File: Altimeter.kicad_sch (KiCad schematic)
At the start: 44 parts, among them U1 ESP32-S3, Y1 40MHz±10ppm

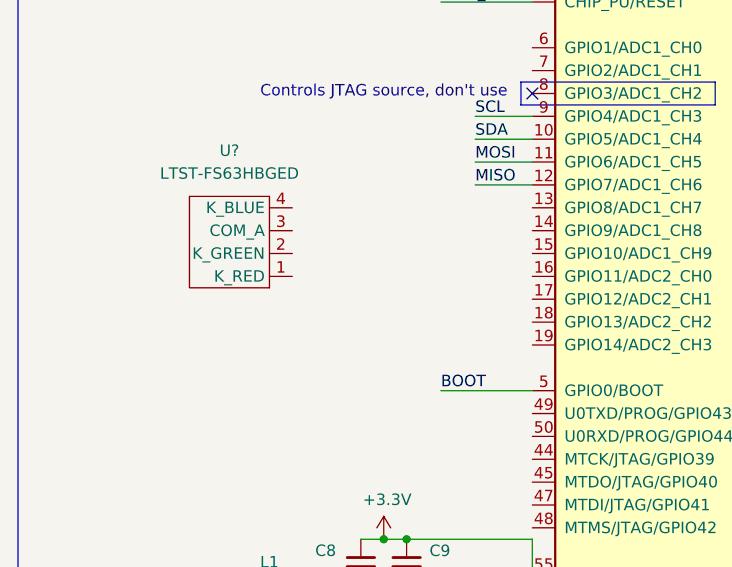
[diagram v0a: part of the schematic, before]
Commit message: added led
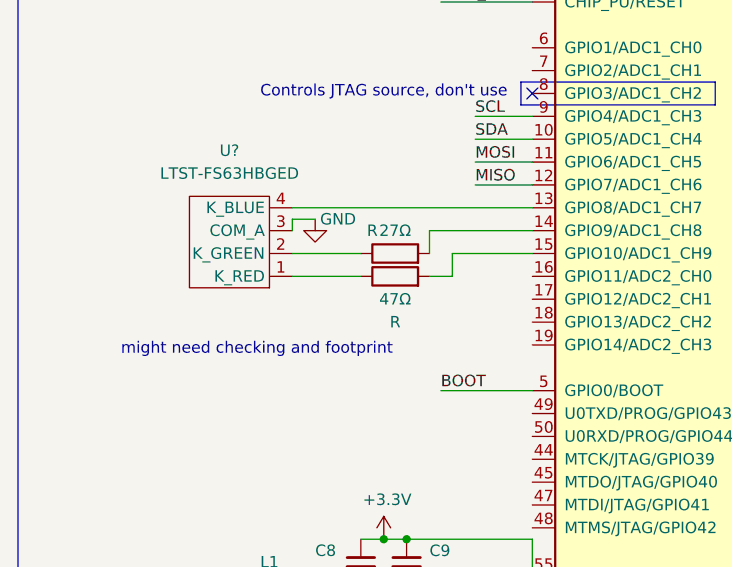
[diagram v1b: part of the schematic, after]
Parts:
- added 27Ω, 47Ω: R, symbol Device:R
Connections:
- net GND: now also U?.3 (COM_A)
- net at U1.13 (GPIO8/ADC1_CH7): now also U?.4 (K_BLUE)
- net at U1.14 (GPIO9/ADC1_CH8): now also 27Ω.2
- net at U1.15 (GPIO10/ADC1_CH9): now also 47Ω.2
- net at U?.1 (K_RED): now also 47Ω.1
- net at U?.2 (K_GREEN): now also 27Ω.1
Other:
- note added: "might need checking and footprint"
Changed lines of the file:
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@@
+    (stroke (width 0) (type default) (color 0 0 0 0))
+  )
+  (wire (pts (xy 43.18 97.79) (xy 50.8 97.79))
     (stroke (width 0) (type default) (color 0 0 0 0))
   )
@@
     (stroke (width 0) (type default) (color 0 0 0 0))
   )
+  (wire (pts (xy 43.18 90.17) (xy 69.85 90.17))
+    (stroke (width 0) (type default) (color 0 0 0 0))
+  )
   (wire (pts (xy 59.69 110.49) (xy 69.85 110.49))
     (stroke (width 0) (type default) (color 0 0 0 0))
@@
     (stroke (width 0) (type default) (color 0 0 0 0))
   )
+  (wire (pts (xy 69.85 92.71) (xy 58.42 92.71))
+    (stroke (width 0) (type default) (color 0 0 0 0))
+  )
   (wire (pts (xy 196.85 139.7) (xy 210.82 139.7))
     (stroke (width 0) (type default) (color 0 0 0 0))
@@
     (stroke (width 0) (type default) (color 0 0 0 0))
   )
+  (wire (pts (xy 60.96 95.25) (xy 60.96 97.79))
+    (stroke (width 0) (type default) (color 0 0 0 0))
+  )
   (wire (pts (xy 62.23 142.24) (xy 69.85 142.24))
     (stroke (width 0) (type default) (color 0 0 0 0))
@@
     (stroke (width 0) (type default) (color 0 0 0 0))
   )
+  (wire (pts (xy 43.18 91.44) (xy 45.72 91.44))
+    (stroke (width 0) (type default) (color 0 0 0 0))
+  )
   (wire (pts (xy 53.34 132.08) (xy 55.88 132.08))
     (stroke (width 0) (type default) (color 0 0 0 0))
@@
     (stroke (width 0) (type default) (color 0 0 0 0))
   )
+  (wire (pts (xy 43.18 92.71) (xy 43.18 91.44))
+    (stroke (width 0) (type default) (color 0 0 0 0))
+  )
   (polyline (pts (xy 124.46 111.76) (xy 124.46 114.3))
     (stroke (width 0) (type default) (color 0 0 0 0))
@@
     (stroke (width 0) (type default) (color 0 0 0 0))
   )
+  (wire (pts (xy 58.42 92.71) (xy 58.42 95.25))
+    (stroke (width 0) (type default) (color 0 0 0 0))
+  )
   (wire (pts (xy 107.95 187.96) (xy 115.57 187.96))
     (stroke (width 0) (type default) (color 0 0 0 0))
@@
     (stroke (width 0) (type default) (color 0 0 0 0))
   )
+  (wire (pts (xy 43.18 95.25) (xy 50.8 95.25))
+    (stroke (width 0) (type default) (color 0 0 0 0))
+  )
   (wire (pts (xy 213.36 62.23) (xy 213.36 96.52))
     (stroke (width 0) (type default) (color 0 0 0 0))
@@
     (stroke (width 0) (type default) (color 0 0 0 0))
   )
+  (wire (pts (xy 58.42 97.79) (xy 60.96 97.79))
+    (stroke (width 0) (type default) (color 0 0 0 0))
+  )
   (wire (pts (xy 63.5 80.01) (xy 69.85 80.01))
     (stroke (width 0) (type default) (color 0 0 0 0))
@@
   )
   (wire (pts (xy 53.34 191.77) (xy 45.72 191.77))
+    (stroke (width 0) (type default) (color 0 0 0 0))
+  )
+  (wire (pts (xy 69.85 95.25) (xy 60.96 95.25))
     (stroke (width 0) (type default) (color 0 0 0 0))
   )
@@
   (text "CAN + is CAN High\nCAN - is CAN LOW\nNamed with a + and - as it\nis a KiCad requirement to\nroute differential tracks\n"
     (at 110.49 167.64 0)
+    (effects (font (size 1.27 1.27)) (justify left bottom))
+  )
+  (text "might need checking and footprint\n" (at 24.13 106.68 0)
     (effects (font (size 1.27 1.27)) (justify left bottom))
   )
@@
     )
     (pin "1")
+  )
+  (symbol (lib_id "Device:R") (at 54.61 97.79 90) (unit 1)
+    (in_bom yes) (on_board yes)
+    (property "Reference" "47Ω" (id 0) (at 54.61 100.33 90))
+    (property "Value" "R" (id 1) (at 54.61 102.87 90))
+    (property "Footprint" "" (id 2) (at 54.61 99.568 90)
+      (effects (font (size 1.27 1.27)) hide)
+    )
+    (property "Datasheet" "~" (id 3) (at 54.61 97.79 0)
+      (effects (font (size 1.27 1.27)) hide)
+    )
+    (pin "1")
+    (pin "2")
   )
   (symbol (lib_id "Device:C_Small") (at 271.78 46.99 0) (unit 1)
@@
     )
     (property "Datasheet" "~" (id 3) (at 34.29 138.43 0)
+      (effects (font (size 1.27 1.27)) hide)
+    )
+    (pin "1")
+    (pin "2")
+  )
+  (symbol (lib_id "Device:R") (at 54.61 95.25 90) (unit 1)
+    (in_bom yes) (on_board yes)
+    (property "Reference" "27Ω" (id 0) (at 54.61 92.71 90))
+    (property "Value" "R" (id 1) (at 52.07 92.71 90))
+    (property "Footprint" "" (id 2) (at 54.61 97.028 90)
+      (effects (font (size 1.27 1.27)) hide)
+    )
+    (property "Datasheet" "~" (id 3) (at 54.61 95.25 0)
       (effects (font (size 1.27 1.27)) hide)
     )
@@
     (pin "1")
   )
+  (symbol (lib_id "power:GND") (at 45.72 91.44 0) (unit 1)
+    (in_bom yes) (on_board yes)
+    (property "Reference" "#PWR?" (id 0) (at 45.72 97.79 0)
+      (effects (font (size 1.27 1.27)) hide)
+    )
+    (property "Value" "GND" (id 1) (at 48.26 91.44 0))
+    (property "Footprint" "" (id 2) (at 45.72 91.44 0)
+      (effects (font (size 1.27 1.27)) hide)
+    )
+    (property "Datasheet" "" (id 3) (at 45.72 91.44 0)
+      (effects (font (size 1.27 1.27)) hide)
+    )
+    (pin "1")
+  )
   (symbol (lib_id "power:GND") (at 213.36 143.51 0) (unit 1)
     (in_bom yes) (on_board yes) (fields_autoplaced)
@@
       (reference "#PWR?") (unit 1) (value "GND") (footprint "")
     )
+    (path "/d1718078-1485-4c9f-b468-a721b1d88ce8"
+      (reference "#PWR?") (unit 1) (value "GND") (footprint "")
+    )
     (path "/dbf2f322-fde2-4da3-b2ce-f14564b17d40"
       (reference "#PWR?") (unit 1) (value "GND") (footprint "")
@@
       (reference "12VLED1") (unit 1) (value "12V_LED") (footprint "Resistor_SMD:R_0402_1005Metric")
     )
+    (path "/7b450b34-c515-464e-aa64-803e3ffdc8aa"
+      (reference "27Ω") (unit 1) (value "R") (footprint "")
+    )
+    (path "/0f205b38-724f-4127-a844-15f920a1a6db"
+      (reference "47Ω") (unit 1) (value "R") (footprint "")
+    )
     (path "/00000000-0000-0000-0000-00005dff8440"

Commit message: final commit pre-review
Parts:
- added 75Ω: R, symbol Device:R
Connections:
- net at U?.4 (K_BLUE): now also 75Ω.1; no longer U1.13 (GPIO8/ADC1_CH7)
- new net: 75Ω.2, U1.13 (GPIO8/ADC1_CH7)
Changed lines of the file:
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@@
-    (stroke (width 0) (type default) (color 0 0 0 0))
-  )
-  (wire (pts (xy 43.18 90.17) (xy 69.85 90.17))
     (stroke (width 0) (type default) (color 0 0 0 0))
   )
@@
     (stroke (width 0) (type default) (color 0 0 0 0))
   )
+  (wire (pts (xy 58.42 90.17) (xy 69.85 90.17))
+    (stroke (width 0) (type default) (color 0 0 0 0))
+  )
   (wire (pts (xy 196.85 139.7) (xy 210.82 139.7))
     (stroke (width 0) (type default) (color 0 0 0 0))
@@
   )
   (wire (pts (xy 20.32 135.89) (xy 29.21 135.89))
+    (stroke (width 0) (type default) (color 0 0 0 0))
+  )
+  (wire (pts (xy 43.18 90.17) (xy 50.8 90.17))
     (stroke (width 0) (type default) (color 0 0 0 0))
   )
@@
   (symbol (lib_id "Device:R") (at 54.61 95.25 90) (unit 1)
     (in_bom yes) (on_board yes)
-    (property "Reference" "27Ω" (id 0) (at 54.61 92.71 90))
+    (property "Reference" "27Ω" (id 0) (at 55.88 92.71 90))
     (property "Value" "R" (id 1) (at 52.07 92.71 90))
     (property "Footprint" "" (id 2) (at 54.61 97.028 90)
@@
     )
     (pin "1")
+  )
+  (symbol (lib_id "Device:R") (at 54.61 90.17 90) (unit 1)
+    (in_bom yes) (on_board yes)
+    (property "Reference" "75Ω" (id 0) (at 55.88 87.63 90))
+    (property "Value" "R" (id 1) (at 52.07 87.63 90))
+    (property "Footprint" "" (id 2) (at 54.61 91.948 90)
+      (effects (font (size 1.27 1.27)) hide)
+    )
+    (property "Datasheet" "~" (id 3) (at 54.61 90.17 0)
+      (effects (font (size 1.27 1.27)) hide)
+    )
+    (pin "1")
+    (pin "2")
   )
   (symbol (lib_id "Device:R_Small") (at 215.9 130.81 180) (unit 1)
@@
       (effects (font (size 1.27 1.27)) hide)
     )
+    (pin "1")
+    (pin "2")
     (pin "3")
     (pin "4")
-    (pin "2")
-    (pin "1")
   )
   (symbol (lib_id "power:GND") (at 45.72 91.44 0) (unit 1)
@@
       (reference "47Ω") (unit 1) (value "R") (footprint "")
     )
+    (path "/83cce8e5-32c1-4f3f-bd78-84e83ca53b42"
+      (reference "75Ω") (unit 1) (value "R") (footprint "")
+    )
     (path "/00000000-0000-0000-0000-00005dff8440"
